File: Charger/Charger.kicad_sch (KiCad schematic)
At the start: 27 parts, among them J1 PL00X-301-10M8, J2 PL00Y-301-10M8, K1 Gigavc PNC11BDA, K2 EV200 HAANA, SW1 Emergency Button, SW2 SW_Push, SW3 SW_Push, U1 ATmega328-A, Y1 20MHz

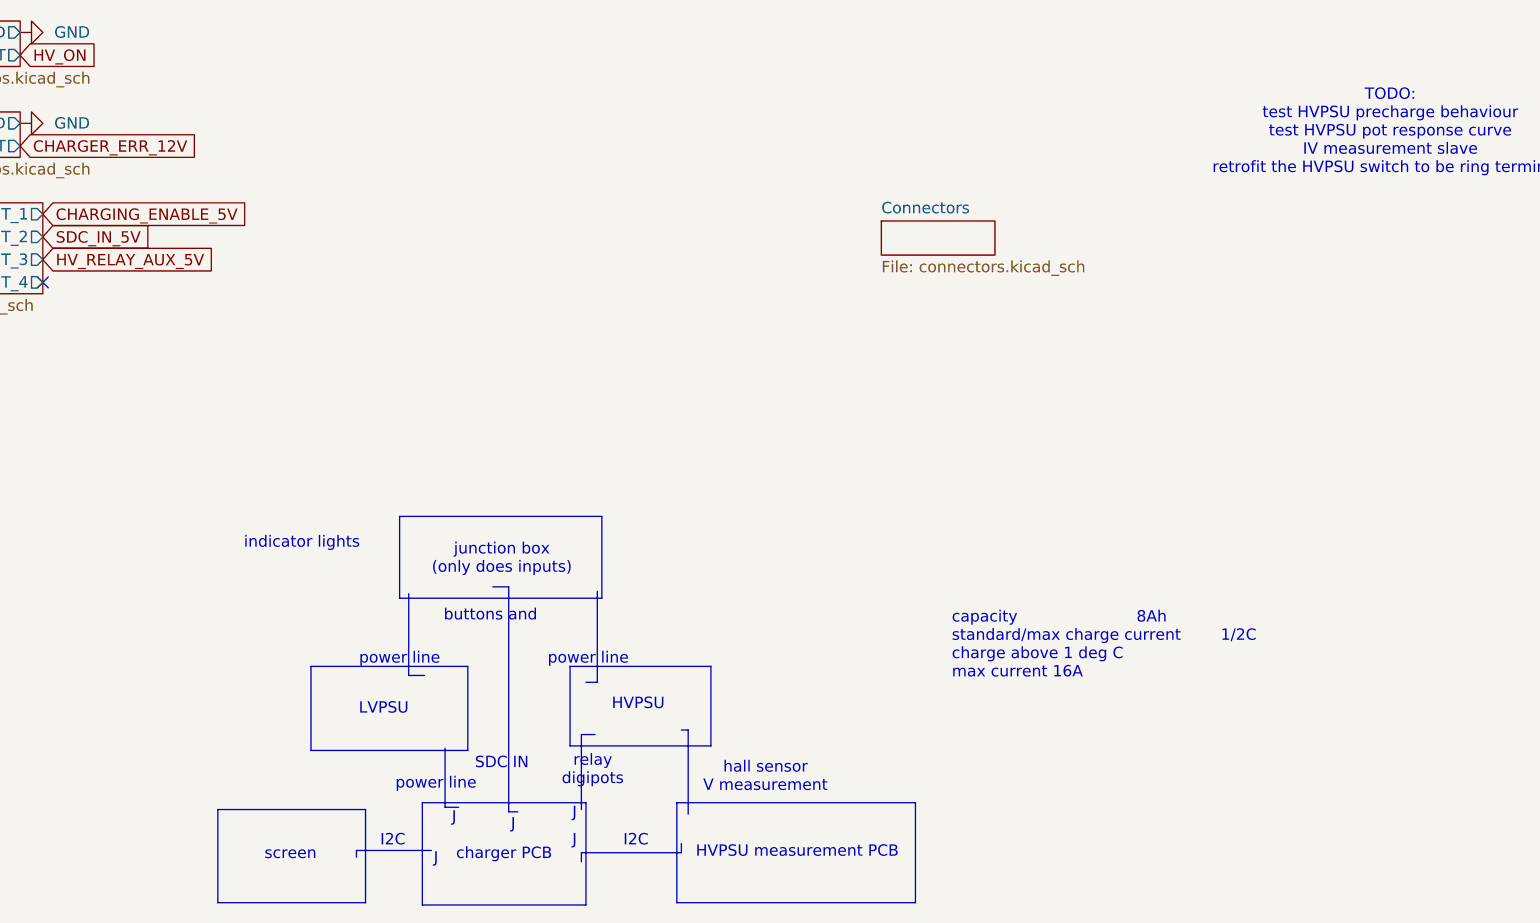
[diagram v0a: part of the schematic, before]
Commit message: Charger schematic WIP
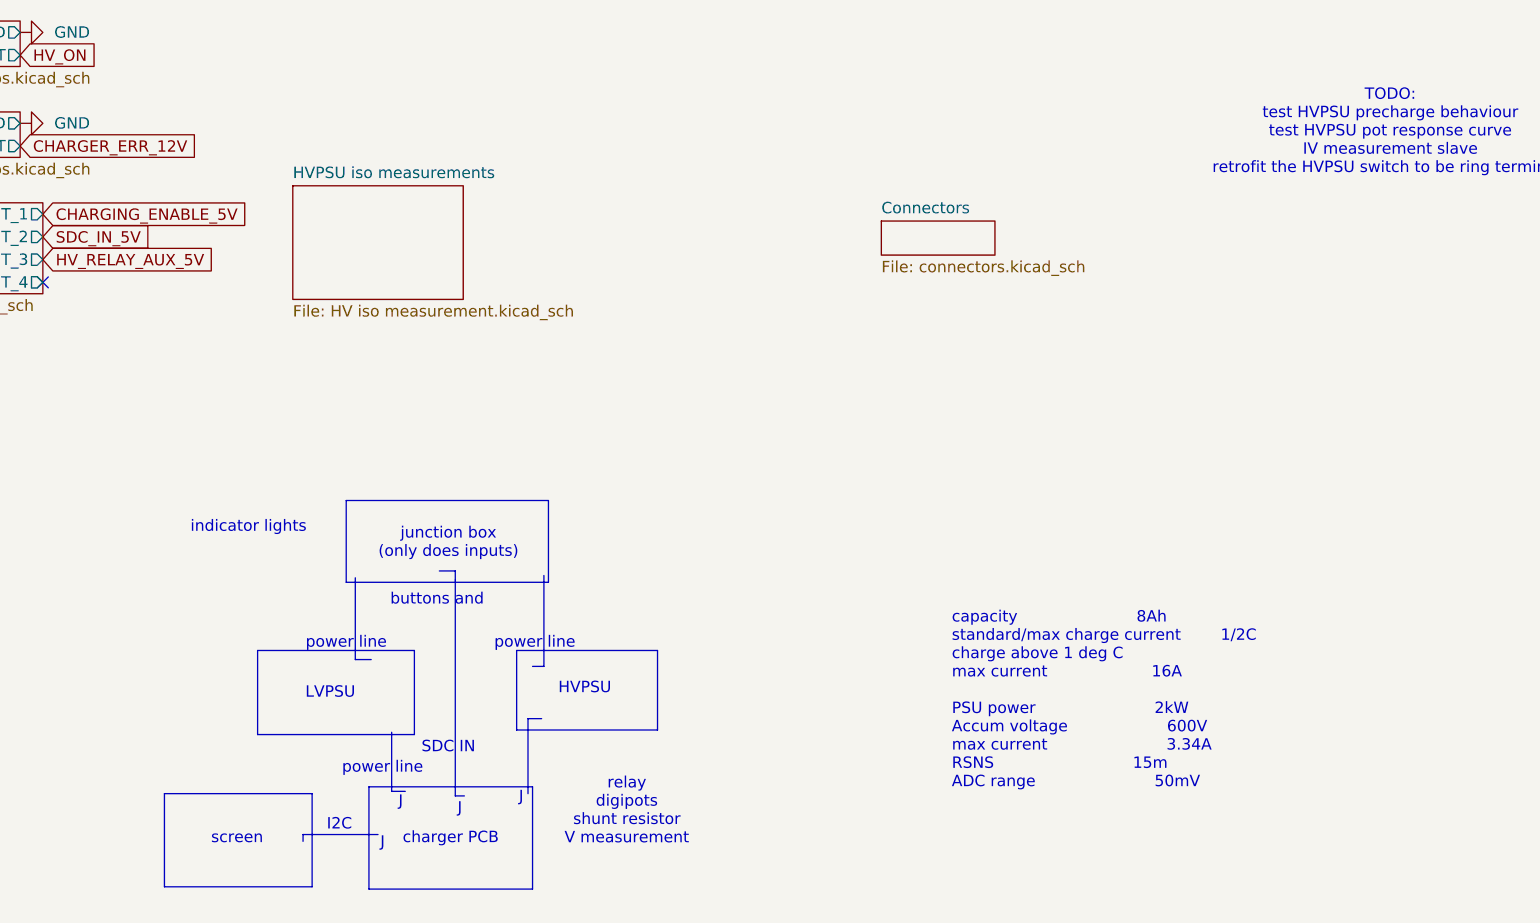
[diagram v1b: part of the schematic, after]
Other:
- added sheet HVPSU iso measurements (HV iso measurement.kicad_sch)
- note added: "capacity 8Ah standard/max charge current 1/2C charge above 1 deg C max current 16A PSU power 2kW Accum voltage 600V max current 3.34A RSNS 15m ADC range 50mV"
- note added: "relay digipots shunt resistor V measurement"
- note removed: "HVPSU measurement PCB"
- note removed: "capacity 8Ah standard/max charge current 1/2C charge above 1 deg C max current 16A"
- note removed: "hall sensor V measurement"
- note removed: "relay digipots"
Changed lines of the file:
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@@
 	(paper "A4")
 	(rectangle
-		(start 109.728 234.696)
-		(end 125.476 243.586)
+		(start 103.759 232.918)
+		(end 119.507 241.808)
 		(stroke
 			(width 0)
@@
 	)
 	(rectangle
-		(start 70.358 250.698)
-		(end 86.868 261.112)
+		(start 64.389 248.92)
+		(end 80.899 259.334)
 		(stroke
 			(width 0)
@@
 	)
 	(rectangle
-		(start 90.678 217.932)
-		(end 113.284 227.076)
+		(start 84.709 216.154)
+		(end 107.315 225.298)
 		(stroke
 			(width 0)
@@
 	)
 	(rectangle
-		(start 93.218 249.936)
-		(end 111.506 261.366)
+		(start 87.249 248.158)
+		(end 105.537 259.588)
 		(stroke
 			(width 0)
@@
 	)
 	(rectangle
-		(start 80.772 234.696)
-		(end 98.298 244.094)
-		(stroke
-			(width 0)
-			(type default)
-		)
-		(fill
-			(type none)
-		)
-	)
-	(rectangle
-		(start 121.666 249.936)
-		(end 148.336 261.112)
+		(start 74.803 232.918)
+		(end 92.329 242.316)
 		(stroke
 			(width 0)
@@
 	(text "J"
 		(exclude_from_sim no)
-		(at 103.378 252.476 0)
+		(at 97.409 250.698 0)
 		(effects
 			(font
@@
 		)
 	)
-	(text "capacity						8Ah\nstandard/max charge current		1/2C\ncharge above 1 deg C\nmax current 16A\n"
+	(text "capacity						8Ah\nstandard/max charge current		1/2C\ncharge above 1 deg C\nmax current 					16A\n\nPSU power						2kW\nAccum voltage					600V\nmax current						3.34A\nRSNS							15m\nADC range						50mV"
 		(exclude_from_sim no)
 		(at 152.4 228.6 0)
@@
 	(text "LVPSU"
 		(exclude_from_sim no)
-		(at 88.9 239.522 0)
+		(at 82.931 237.744 0)
 		(effects
 			(font
@@
 	(text "J"
 		(exclude_from_sim no)
-		(at 110.236 251.206 0)
+		(at 104.267 249.428 0)
 		(effects
 			(font
@@
 	(text "screen"
 		(exclude_from_sim no)
-		(at 78.486 255.778 0)
+		(at 72.517 254 0)
 		(effects
 			(font
@@
 		)
 	)
-	(text "I2C"
-		(exclude_from_sim no)
-		(at 117.094 254.254 0)
-		(effects
-			(font
-				(size 1.27 1.27)
-			)
-		)
-	)
 	(text "buttons and"
 		(exclude_from_sim no)
-		(at 100.838 229.108 0)
+		(at 94.869 227.33 0)
 		(effects
 			(font
@@
 		)
 	)
-	(text "hall sensor\nV measurement"
-		(exclude_from_sim no)
-		(at 131.572 247.142 0)
-		(effects
-			(font
-				(size 1.27 1.27)
-			)
-		)
-	)
 	(text "charger PCB"
 		(exclude_from_sim no)
-		(at 102.362 255.778 0)
+		(at 96.393 254 0)
 		(effects
 			(font
@@
 		)
 	)
-	(text "J"
-		(exclude_from_sim no)
-		(at 110.236 254.254 0)
-		(effects
-			(font
-				(size 1.27 1.27)
-			)
-		)
-	)
 	(text "(Arduino A2)\n"
 		(exclude_from_sim no)
@@
 		)
 	)
-	(text "HVPSU measurement PCB"
-		(exclude_from_sim no)
-		(at 135.128 255.524 0)
-		(effects
-			(font
-				(size 1.27 1.27)
-			)
-		)
-	)
 	(text "INDICATORS\nTSALG\nAMS ERR\nIMD ERR\nCHARGER ERR"
 		(exclude_from_sim no)
@@
 	(text "J"
 		(exclude_from_sim no)
-		(at 96.774 251.714 0)
+		(at 90.805 249.936 0)
 		(effects
 			(font
@@
 	(text "I2C"
 		(exclude_from_sim no)
-		(at 89.916 254.254 0)
+		(at 83.947 252.476 0)
 		(effects
 			(font
@@
 	(text "power line"
 		(exclude_from_sim no)
-		(at 111.76 233.934 0)
+		(at 105.791 232.156 0)
 		(effects
 			(font
@@
 	(text "HVPSU"
 		(exclude_from_sim no)
-		(at 117.348 239.014 0)
+		(at 111.379 237.236 0)
 		(effects
 			(font
@@
 	(text "junction box\n(only does inputs)"
 		(exclude_from_sim no)
-		(at 102.108 222.758 0)
+		(at 96.139 220.98 0)
 		(effects
 			(font
@@
 	(text "power line"
 		(exclude_from_sim no)
-		(at 94.742 247.904 0)
+		(at 88.773 246.126 0)
 		(effects
 			(font
@@
 	(text "J"
 		(exclude_from_sim no)
-		(at 94.742 256.286 0)
+		(at 88.773 254.508 0)
 		(effects
 			(font
@@
 	(text "power line"
 		(exclude_from_sim no)
-		(at 90.678 233.934 0)
+		(at 84.709 232.156 0)
 		(effects
 			(font
@@
 	(text "SDC IN"
 		(exclude_from_sim no)
-		(at 102.108 245.618 0)
+		(at 96.139 243.84 0)
 		(effects
 			(font
@@
 		)
 	)
-	(text "relay\ndigipots"
+	(text "relay\ndigipots\nshunt resistor\nV measurement"
 		(exclude_from_sim no)
-		(at 112.268 246.38 0)
+		(at 116.078 250.952 0)
 		(effects
 			(font
@@
 	(text "indicator lights"
 		(exclude_from_sim no)
-		(at 79.756 220.98 0)
+		(at 73.787 219.202 0)
 		(effects
 			(font
@@
 	(polyline
 		(pts
-			(xy 85.852 255.27) (xy 85.852 256.032)
+			(xy 79.883 253.492) (xy 79.883 254.254)
 		)
 		(stroke
@@
 	(polyline
 		(pts
-			(xy 122.174 254.508) (xy 122.174 255.524)
-		)
-		(stroke
-			(width 0)
-			(type default)
-		)
-	)
-	(polyline
-		(pts
-			(xy 122.174 241.808) (xy 122.936 241.808)
-		)
-		(stroke
-			(width 0)
-			(type default)
-		)
-	)
-	(polyline
-		(pts
-			(xy 91.694 226.568) (xy 91.694 235.712)
+			(xy 85.725 224.79) (xy 85.725 233.934)
 		)
 		(stroke
@@
 	(polyline
 		(pts
-			(xy 111.506 236.474) (xy 112.776 236.474)
+			(xy 105.537 234.696) (xy 106.807 234.696)
 		)
 		(stroke
@@
 	(polyline
 		(pts
-			(xy 102.87 226.822) (xy 102.87 250.952)
+			(xy 96.901 225.044) (xy 96.901 249.174)
 		)
 		(stroke
@@
 	(polyline
 		(pts
-			(xy 112.776 226.314) (xy 112.776 236.474)
+			(xy 106.807 224.536) (xy 106.807 234.696)
 		)
 		(stroke
@@
 	(polyline
 		(pts
-			(xy 95.758 250.444) (xy 97.282 250.444)
+			(xy 89.789 248.666) (xy 91.313 248.666)
 		)
 		(stroke
@@
 	(polyline
 		(pts
-			(xy 102.87 226.822) (xy 102.87 225.806)
+			(xy 96.901 225.044) (xy 96.901 224.028)
 		)
 		(stroke
@@
 	(polyline
 		(pts
-			(xy 110.998 242.316) (xy 110.998 250.698)
+			(xy 105.029 240.538) (xy 105.029 248.92)
 		)
 		(stroke
@@
 	(polyline
 		(pts
-			(xy 94.234 255.27) (xy 85.852 255.27)
+			(xy 88.265 253.492) (xy 79.883 253.492)
 		)
 		(stroke
@@
 		)
 	)
-	(polyline
-		(pts
-			(xy 122.936 241.808) (xy 122.936 251.206)
-		)
-		(stroke
-			(width 0)
-			(type default)
-		)
-	)
 	(wire
 		(pts
@@
 		)
 	)
-	(polyline
-		(pts
-			(xy 110.998 255.524) (xy 122.174 255.524)
-		)
-		(stroke
-			(width 0)
-			(type default)
-		)
-	)
 	(wire
 		(pts
@@
 	(polyline
 		(pts
-			(xy 101.092 225.806) (xy 102.87 225.806)
+			(xy 95.123 224.028) (xy 96.901 224.028)
 		)
 		(stroke
@@
 		)
 	)
-	(polyline
-		(pts
-			(xy 110.998 255.524) (xy 110.998 256.54)
-		)
-		(stroke
-			(width 0)
-			(type default)
-		)
-	)
 	(wire
 		(pts
@@
 	(polyline
 		(pts
-			(xy 91.694 235.712) (xy 93.472 235.712)
+			(xy 85.725 233.934) (xy 87.503 233.934)
 		)
 		(stroke
@@
 	(polyline
 		(pts
-			(xy 110.998 242.316) (xy 112.522 242.316)
+			(xy 105.029 240.538) (xy 106.553 240.538)
 		)
 		(stroke
@@
 	(polyline
 		(pts
-			(xy 102.87 250.952) (xy 103.886 250.952)
+			(xy 96.901 249.174) (xy 97.917 249.174)
 		)
 		(stroke
@@
 	(polyline
 		(pts
-			(xy 95.758 243.84) (xy 95.758 250.444)
+			(xy 89.789 242.062) (xy 89.789 248.666)
 		)
 		(stroke
@@
 				)
 			)
+		)
+	)
+	(sheet
+		(at 78.74 180.975)
+		(size 19.05 12.7)
+		(exclude_from_sim no)
+		(in_bom yes)
+		(on_board yes)
+		(dnp no)
+		(fields_autoplaced yes)
+		(stroke
+			(width 0.1524)
+			(type solid)
+		)
+		(fill
+			(color 0 0 0 0)
+		)
+		(property "Sheetname" "HVPSU iso measurements"
+			(at 78.74 180.2634 0)
+			(show_name no)
+			(do_not_autoplace no)
+			(effects
+				(font
+					(size 1.27 1.27)
+				)
+				(justify left bottom)
+			)
+		)
+		(property "Sheetfile" "HV iso measurement.kicad_sch"
+			(at 78.74 194.2596 0)
+			(show_name no)
+			(do_not_autoplace no)
+			(effects
+				(font
+					(size 1.27 1.27)
+				)
+				(justify left top)
+			)
+		)
+		(instances
+			(project "Charger"
+				(path "/ba218c5d-b6ee-4635-9cf5-de406e83bbdf"
+					(page "9")
+				)
+			)
